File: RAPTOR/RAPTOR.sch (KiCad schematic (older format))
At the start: 49 parts, among them J1 SOLC_CONN, J10 EXT_LED3, J11 SRVOL_CONN, J12 SRVOR_CONN, J13 HOTWIRE_CONN, J14 RBF_CONN, J15 EEPROM_BTN_CONN, J16 SOLC_SW_CONN, J17 SOLP_SW_CONN, J18 CONN_BUZZER, J2 SOLP_CONN, J3 JST_2MM_MALE, J4 CONN_LED_FIX, J5 CONN_SOLP_LED, J6 CONN_SOLC_LED, J7 EXT_LED0, J8 EXT_LED1, J9 EXT_LED2, P1 Power, P2 Analog, P3 Digital, P4 Digital, P5 CONN_01X01, P6 CONN_01X01, P7 CONN_01X01, P8 CONN_01X01, Q1 MOSFET-NCH-STQ2NK60ZR-AP, Q2 MOSFET-NCH-STQ2NK60ZR-AP, Q3 MOSFET-NCH-STQ2NK60ZR-AP, Q4 MOSFET-NCH-STQ2NK60ZR-AP, Q5 MOSFET-NCH-STQ2NK60ZR-AP, U1 BMP280 Breakout, U2 BNO055 Breakout, U3 OpenLog, U4 AdafruitGPS, U5 U3V12F12, U6 D24V550F5

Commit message: do schematic for thunderbird
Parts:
- removed D8, D9: DIODE-1N4148, Silicon-Custom:DIODE-1N4148, symbol RAPTOR-rescue:DIODE-1N4148-SparkFun-DiscreteSemi
- removed J1: SOLC_CONN, RAPTOR_footprints:Molex-2pin, symbol RAPTOR-rescue:CONN_02-SparkFun-Connectors
- removed J12: SRVOR_CONN, RAPTOR_footprints:Molex-MOTOR, symbol RAPTOR-rescue:CONN_03-SparkFun-Connectors
- removed J13: HOTWIRE_CONN, RAPTOR_footprints:Molex-2pin, symbol RAPTOR-rescue:CONN_02-SparkFun-Connectors
- removed J16: SOLC_SW_CONN, RAPTOR_footprints:Molex-2pin, symbol RAPTOR-rescue:CONN_02-SparkFun-Connectors
- removed J17: SOLP_SW_CONN, RAPTOR_footprints:Molex-2pin, symbol RAPTOR-rescue:CONN_02-SparkFun-Connectors
- removed J2: SOLP_CONN, RAPTOR_footprints:Molex-2pin, symbol RAPTOR-rescue:CONN_02-SparkFun-Connectors
- removed J4: CONN_LED_FIX, RAPTOR_footprints:Molex-2pin, symbol RAPTOR-rescue:CONN_02-SparkFun-Connectors
- removed J5: CONN_SOLP_LED, RAPTOR_footprints:Molex-2pin, symbol RAPTOR-rescue:CONN_02-SparkFun-Connectors
- removed J6: CONN_SOLC_LED, RAPTOR_footprints:Molex-2pin, symbol RAPTOR-rescue:CONN_02-SparkFun-Connectors
- removed JP1, JP2: Jumper, symbol Device:Jumper
- removed P1: Power, RAPTOR_footprints:Socket_Strip_Arduino_1x08, symbol Connector_Generic:Conn_01x08
- removed P2: Analog, RAPTOR_footprints:Arduino_Analog_06, symbol RAPTOR-rescue:Arduino_Analog_Conn
- removed P3: Digital, RAPTOR_footprints:Arduino_x10_Digital, symbol RAPTOR-rescue:Arduino_Digital_01x10_Conn
- removed P4: Digital, RAPTOR_footprints:Arduino_x08_Digital, symbol RAPTOR-rescue:Arduino_Digital_8
- removed P5, P6, P7, P8: CONN_01X01, Socket_Arduino_Uno:Arduino_1pin, symbol Connector_Generic:Conn_01x01
- removed Q1, Q2, Q5: MOSFET-NCH-STQ2NK60ZR-AP, RAPTOR_footprints:MOSFET, symbol RAPTOR-rescue:MOSFET-NCH-2N7002PW-SparkFun-DiscreteSemi
- removed R2, R3, R4: 100OHM-0603-1_10W-1%, RAPTOR_footprints:Resistor, symbol RAPTOR-rescue:100OHM-0603-1_10W-1%-SparkFun-Resistors
- removed R6, R7, R8: 4.7KOHM-0603-1_10W-1%, RAPTOR_footprints:Resistor, symbol RAPTOR-rescue:4.7KOHM-0603-1_10W-1%-SparkFun-Resistors
- removed U1: BMP280 Breakout, RAPTOR_footprints:BMP280, symbol RAPTOR-rescue:BMP280-bmp280
- removed U2: BNO055 Breakout, RAPTOR_footprints:BNO055, symbol RAPTOR-rescue:BNO055-bno055
- removed U3: OpenLog, RAPTOR_footprints:OpenLog, symbol RAPTOR-rescue:OpenLog-openlog
- removed U5: U3V12F12, RAPTOR_footprints:U3V12F12, symbol RAPTOR-rescue:U3V12F12
- added A?: Arduino_Nano_v3.x, Module:Arduino_Nano, symbol MCU_Module:Arduino_Nano_v3.x
- added U?: microsd, symbol RAPTOR-rescue:microsd
- J11: value SRVOL_CONN -> SRVO_CONN
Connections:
- net labels added: MISO, MOSI, SCK, SRVO, SS
- net labels removed: +12V, A4(SDA), A5(SCL), AREF, HOTWIRE, I2C_SCL, I2C_SDA, IOREF, LEDC_DTA, LEDP_DTA, Reset, SD_RX, SD_TX, SOLC_DTA, SOLC_SW, SOLP_DTA, SOLP_SW, SRVO_L, SRVO_R
- wire segments 182 -> 83
- no-connect marks 18 -> 6
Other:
- note removed: "1"
- note removed: "Holes"
- note removed: "Shield for Arduino that uses\nthe same pin disposition\nlike "Uno" board Rev 3."
- moved on the sheet: J10, J11, J14, J15, J18, J3, J7, J8, J9, Q3, Q4, R1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

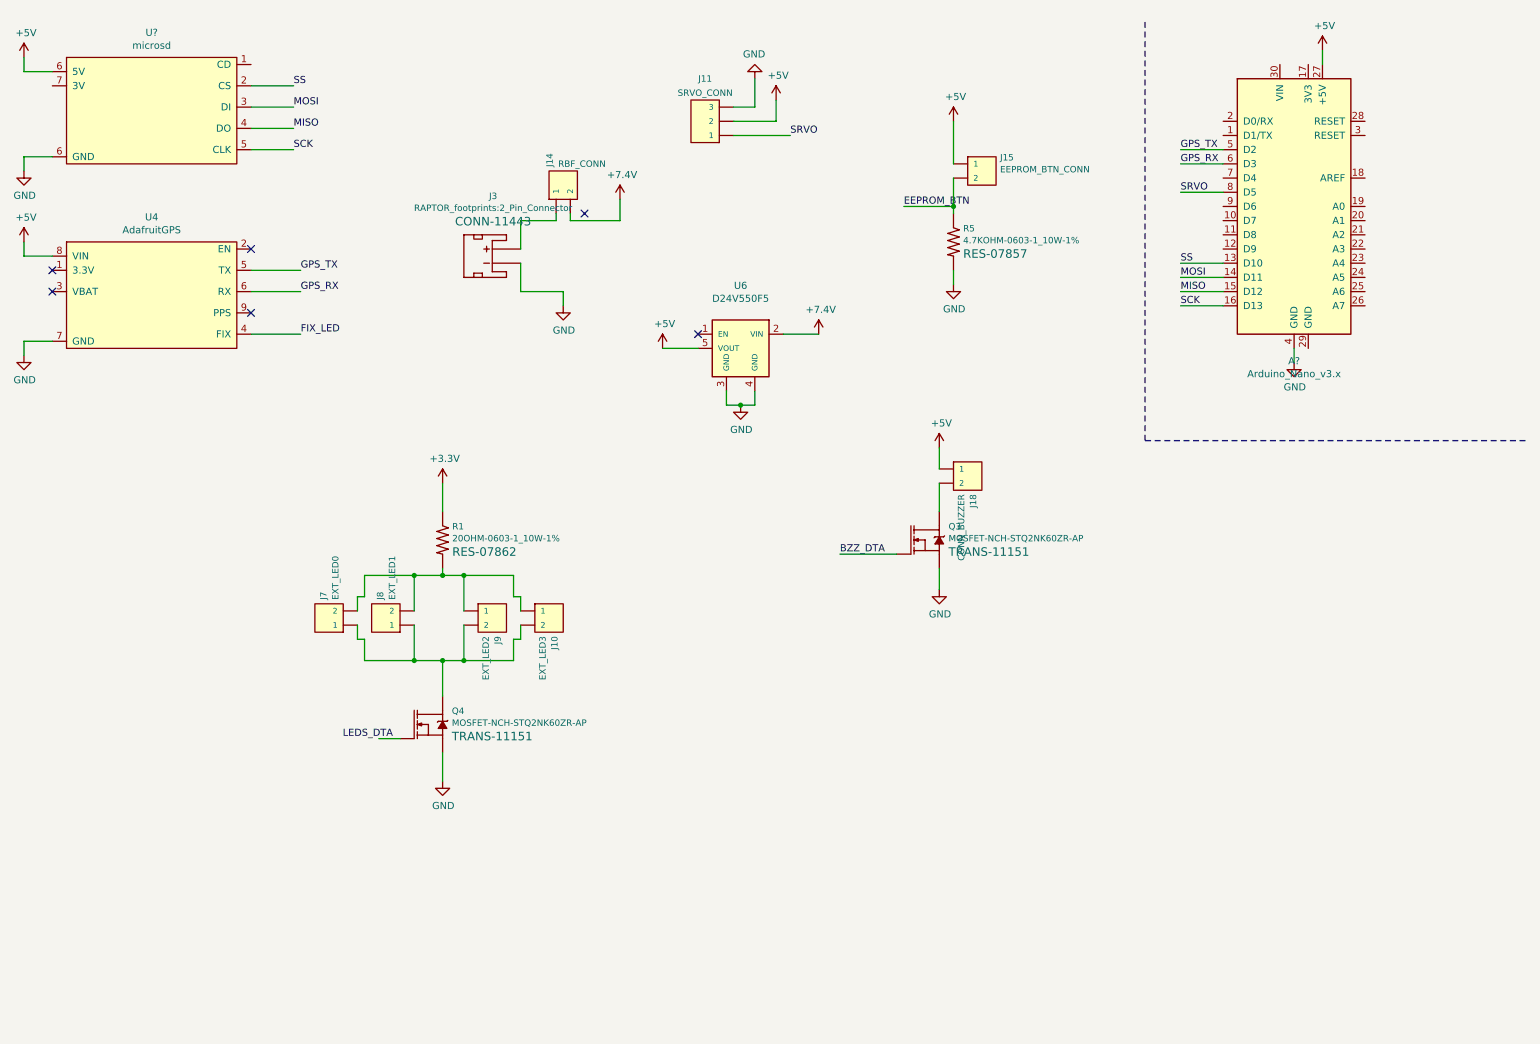
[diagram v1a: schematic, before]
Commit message: update schematic, remove some leds and eeprom button
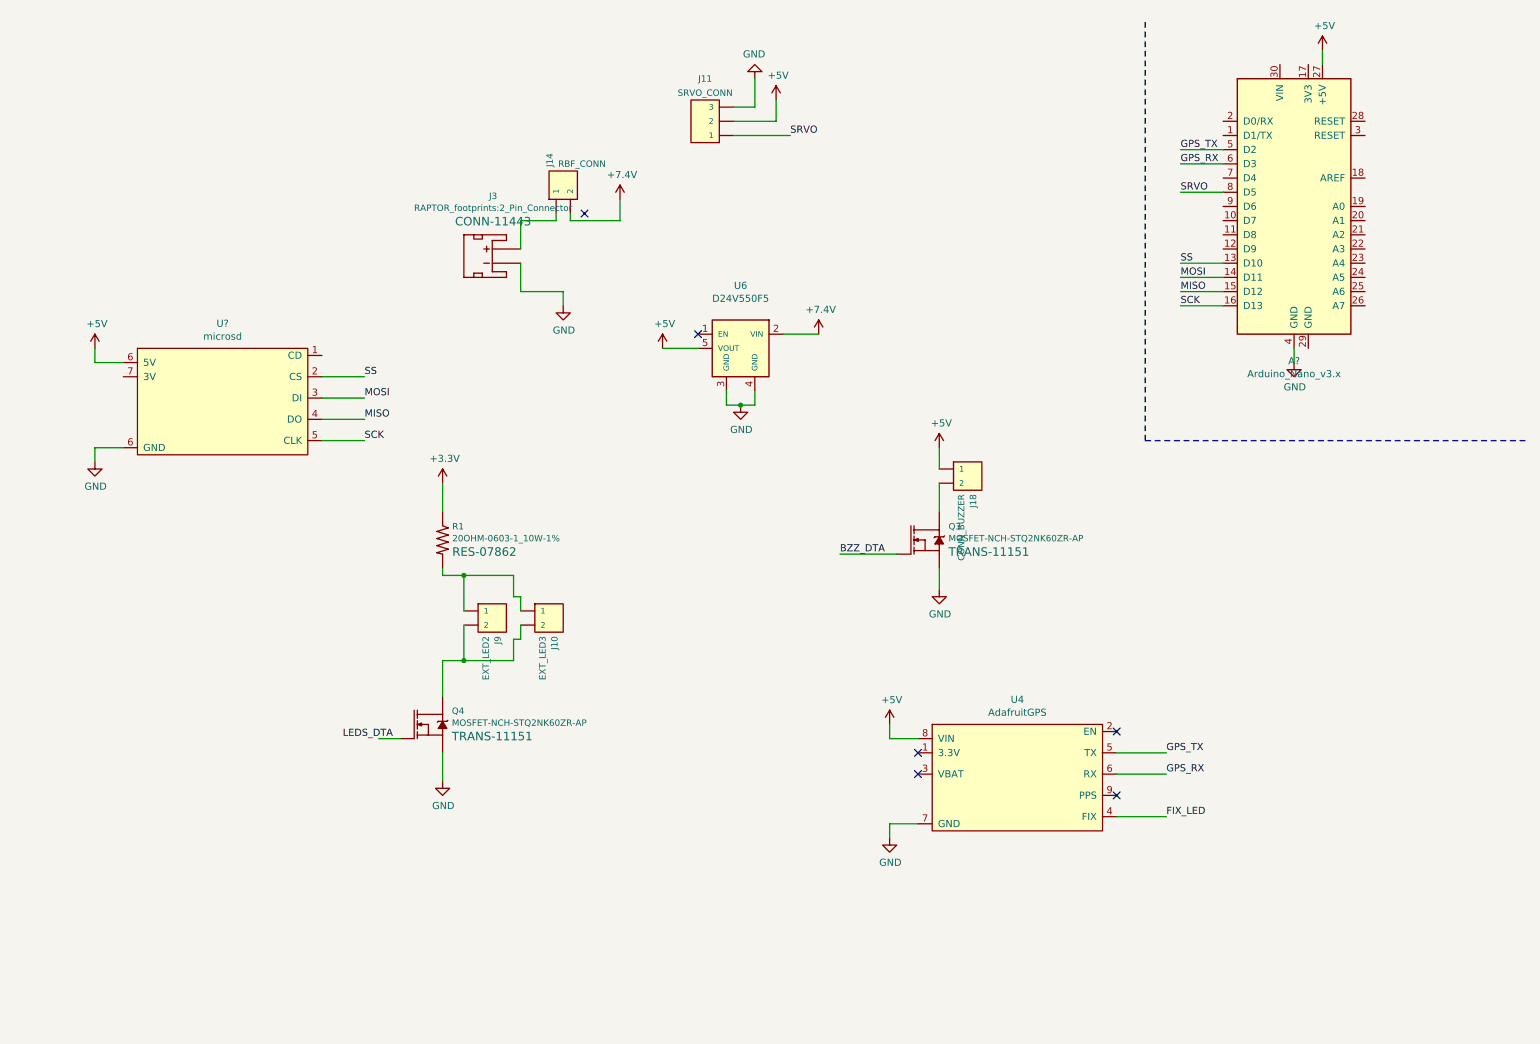
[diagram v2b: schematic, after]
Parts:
- removed J15: EEPROM_BTN_CONN, RAPTOR_footprints:Molex-2pin, symbol RAPTOR-rescue:CONN_02-SparkFun-Connectors
- removed J7: EXT_LED0, RAPTOR_footprints:Molex-2pin, symbol RAPTOR-rescue:CONN_02-SparkFun-Connectors
- removed J8: EXT_LED1, RAPTOR_footprints:Molex-2pin, symbol RAPTOR-rescue:CONN_02-SparkFun-Connectors
- removed R5: 4.7KOHM-0603-1_10W-1%, RAPTOR_footprints:Resistor, symbol RAPTOR-rescue:4.7KOHM-0603-1_10W-1%-SparkFun-Resistors
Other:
- moved on the sheet: U4, U?
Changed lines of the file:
@@
 L RAPTOR-rescue:AdafruitGPS-adafruitgps U4
 U 1 1 5BDE25E6
-P 1500 2400
-F 0 "U4" H 1500 2925 50  0000 C CNN
-F 1 "AdafruitGPS" H 1500 2834 50  0000 C CNN
-F 2 "RAPTOR_footprints:AdafruitGPS" H 1600 2350 50  0001 C CNN
-F 3 "https://learn.adafruit.com/adafruit-ultimate-gps" H 1600 2350 50  0001 C CNN
-	1    1500 2400
+P 7600 5800
+F 0 "U4" H 7600 6325 50  0000 C CNN
+F 1 "AdafruitGPS" H 7600 6234 50  0000 C CNN
+F 2 "RAPTOR_footprints:AdafruitGPS" H 7700 5750 50  0001 C CNN
+F 3 "https://learn.adafruit.com/adafruit-ultimate-gps" H 7700 5750 50  0001 C CNN
+	1    7600 5800
 	1    0    0    -1
 $EndComp
@@
 L power:GND #PWR0106
 U 1 1 5BDE7CE6
-P 600 2850
-F 0 "#PWR0106" H 600 2600 50  0001 C CNN
-F 1 "GND" H 605 2677 50  0000 C CNN
-F 2 "" H 600 2850 50  0001 C CNN
-F 3 "" H 600 2850 50  0001 C CNN
-	1    600  2850
-	1    0    0    -1
-$EndComp
-Wire Wire Line
-	800  2750 600  2750
-Wire Wire Line
-	600  2750 600  2850
+P 6700 6250
+F 0 "#PWR0106" H 6700 6000 50  0001 C CNN
+F 1 "GND" H 6705 6077 50  0000 C CNN
+F 2 "" H 6700 6250 50  0001 C CNN
+F 3 "" H 6700 6250 50  0001 C CNN
+	1    6700 6250
+	1    0    0    -1
+$EndComp
+Wire Wire Line
+	6900 6150 6700 6150
+Wire Wire Line
+	6700 6150 6700 6250
 $Comp
 L power:+5V #PWR0107
 U 1 1 5BDE90FA
-P 600 2050
-F 0 "#PWR0107" H 600 1900 50  0001 C CNN
-F 1 "+5V" H 615 2223 50  0000 C CNN
-F 2 "" H 600 2050 50  0001 C CNN
-F 3 "" H 600 2050 50  0001 C CNN
-	1    600  2050
-	1    0    0    -1
-$EndComp
-Wire Wire Line
-	600  2050 600  2150
-Wire Wire Line
-	600  2150 800  2150
-Text Label 2550 2250 0    50   ~ 0
+P 6700 5450
+F 0 "#PWR0107" H 6700 5300 50  0001 C CNN
+F 1 "+5V" H 6715 5623 50  0000 C CNN
+F 2 "" H 6700 5450 50  0001 C CNN
+F 3 "" H 6700 5450 50  0001 C CNN
+	1    6700 5450
+	1    0    0    -1
+$EndComp
+Wire Wire Line
+	6700 5450 6700 5550
+Wire Wire Line
+	6700 5550 6900 5550
+Text Label 8650 5650 0    50   ~ 0
 GPS_TX
 Wire Wire Line
-	2200 2250 2550 2250
-Text Label 2550 2400 0    50   ~ 0
+	8300 5650 8650 5650
+Text Label 8650 5800 0    50   ~ 0
 GPS_RX
 Wire Wire Line
-	2200 2400 2550 2400
-Text Label 2550 2700 0    50   ~ 0
+	8300 5800 8650 5800
+Text Label 8650 6100 0    50   ~ 0
 FIX_LED
 Wire Wire Line
-	2200 2700 2550 2700
-NoConn ~ 800  2250
-NoConn ~ 800  2400
-NoConn ~ 2200 2550
-NoConn ~ 2200 2100
+	8300 6100 8650 6100
+NoConn ~ 6900 5650
+NoConn ~ 6900 5800
+NoConn ~ 8300 5950
+NoConn ~ 8300 5500
 Text Label 6000 1300 0    50   ~ 0
 SRVO
@@
 	4100 1900 4100 2100
 $Comp
-L power:+5V #PWR021
-U 1 1 5C539DC6
-P 7150 1200
-F 0 "#PWR021" H 7150 1050 50  0001 C CNN
-F 1 "+5V" H 7165 1373 50  0000 C CNN
-F 2 "" H 7150 1200 50  0001 C CNN
-F 3 "" H 7150 1200 50  0001 C CNN
-	1    7150 1200
-	1    0    0    -1
-$EndComp
-$Comp
-L power:GND #PWR022
-U 1 1 5C539DCC
-P 7150 2350
-F 0 "#PWR022" H 7150 2100 50  0001 C CNN
-F 1 "GND" H 7155 2177 50  0000 C CNN
-F 2 "" H 7150 2350 50  0001 C CNN
-F 3 "" H 7150 2350 50  0001 C CNN
-	1    7150 2350
-	1    0    0    -1
-$EndComp
-$Comp
-L RAPTOR-rescue:4.7KOHM-0603-1_10W-1%-SparkFun-Resistors R5
-U 1 1 5C539DD3
-P 7150 2050
-F 0 "R5" V 7055 2118 45  0000 L CNN
-F 1 "4.7KOHM-0603-1_10W-1%" V 7139 2118 45  0000 L CNN
-F 2 "RAPTOR_footprints:Resistor" H 7150 2200 20  0001 C CNN
-F 3 "" H 7150 2050 60  0001 C CNN
-F 4 "RES-07857" V 7234 2118 60  0000 L CNN "Field4"
-	1    7150 2050
-	0    1    1    0
-$EndComp
-Wire Wire Line
-	7150 2250 7150 2350
-$Comp
 L RAPTOR-rescue:CONN_03-SparkFun-Connectors J11
 U 1 1 5C6B1587
@@
 	3700 5000 4050 5000
 Wire Wire Line
-	3000 4850 3000 5000
-Wire Wire Line
-	3000 5000 3350 5000
-Connection ~ 3350 5000
-Wire Wire Line
-	3000 4550 3000 4400
-Wire Wire Line
-	3000 4400 3350 4400
-Wire Wire Line
 	3550 4400 3550 4350
-Connection ~ 3350 4400
-Wire Wire Line
-	3350 4400 3550 4400
 Wire Wire Line
 	3700 4400 3550 4400
-Connection ~ 3550 4400
 Wire Wire Line
 	4050 4550 4050 4400
@@
 	-1   0    0    1
 $EndComp
-$Comp
-L RAPTOR-rescue:CONN_02-SparkFun-Connectors J8
-U 1 1 5C557DC0
-P 3250 4750
-F 0 "J8" V 3111 4928 45  0000 L CNN
-F 1 "EXT_LED1" V 3195 4928 45  0000 L CNN
-F 2 "RAPTOR_footprints:Molex-2pin" H 3250 5000 20  0001 C CNN
-F 3 "" H 3250 4750 50  0001 C CNN
-F 4 "XXX-00000" V 3290 4928 60  0001 L CNN "Field4"
-	1    3250 4750
-	1    0    0    -1
-$EndComp
-$Comp
-L RAPTOR-rescue:CONN_02-SparkFun-Connectors J7
-U 1 1 5C5688B4
-P 2850 4750
-F 0 "J7" V 2711 4928 45  0000 L CNN
-F 1 "EXT_LED0" V 2795 4928 45  0000 L CNN
-F 2 "RAPTOR_footprints:Molex-2pin" H 2850 5000 20  0001 C CNN
-F 3 "" H 2850 4750 50  0001 C CNN
-F 4 "XXX-00000" V 2890 4928 60  0001 L CNN "Field4"
-	1    2850 4750
-	1    0    0    -1
-$EndComp
 Wire Wire Line
 	4050 4550 4100 4550
@@
 	4100 4850 4100 4750
 Wire Wire Line
-	3000 4550 2950 4550
-Wire Wire Line
-	2950 4550 2950 4650
-Wire Wire Line
-	3000 4850 2950 4850
-Wire Wire Line
-	2950 4850 2950 4750
-Wire Wire Line
 	3700 4400 3700 4650
 Wire Wire Line
-	3350 4400 3350 4650
-Wire Wire Line
-	3350 4750 3350 5000
-Wire Wire Line
 	3700 4750 3700 5000
 Wire Wire Line
-	3350 5000 3550 5000
-Wire Wire Line
 	3550 5000 3550 5250
-Connection ~ 3550 5000
 Wire Wire Line
 	3550 5000 3700 5000
 Wire Wire Line
 	3550 5650 3550 5850
-$Comp
-L RAPTOR-rescue:CONN_02-SparkFun-Connectors J15
-U 1 1 5C767459
-P 7250 1500
-F 0 "J15" H 7022 1455 45  0000 R CNN
-F 1 "EEPROM_BTN_CONN" H 7022 1539 45  0000 R CNN
-F 2 "RAPTOR_footprints:Molex-2pin" H 7250 1750 20  0001 C CNN
-F 3 "" H 7250 1500 50  0001 C CNN
-F 4 "XXX-00000" H 7022 1634 60  0001 R CNN "Field4"
-	1    7250 1500
-	-1   0    0    1
-$EndComp
-Wire Wire Line
-	7150 1200 7150 1500
 NoConn ~ 4550 1850
 Wire Wire Line
@@
 	1    0    0    -1
 $EndComp
-Wire Wire Line
-	7150 1800 7150 1850
-Connection ~ 7150 1800
-Wire Wire Line
-	6800 1800 7150 1800
-Text Label 6800 1800 0    50   ~ 0
-EEPROM_BTN
 $Comp
 L RAPTOR-rescue:microsd U?
 U 1 1 5D34E005
-P 1500 1100
-F 0 "U?" H 1500 1625 50  0000 C CNN
-F 1 "microsd" H 1500 1534 50  0000 C CNN
-F 2 "" H 1500 1500 50  0001 C CNN
-F 3 "" H 1500 1500 50  0001 C CNN
-	1    1500 1100
-	1    0    0    -1
-$EndComp
-Wire Wire Line
-	600  850  800  850
+P 2000 3150
+F 0 "U?" H 2000 3675 50  0000 C CNN
+F 1 "microsd" H 2000 3584 50  0000 C CNN
+F 2 "" H 2000 3550 50  0001 C CNN
+F 3 "" H 2000 3550 50  0001 C CNN
+	1    2000 3150
+	1    0    0    -1
+$EndComp
+Wire Wire Line
+	1100 2900 1300 2900
 $Comp
 L power:GND #PWR?
 U 1 1 5D361F5D
-P 600 1550
-F 0 "#PWR?" H 600 1300 50  0001 C CNN
-F 1 "GND" H 605 1377 50  0000 C CNN
-F 2 "" H 600 1550 50  0001 C CNN
-F 3 "" H 600 1550 50  0001 C CNN
-	1    600  1550
-	1    0    0    -1
-$EndComp
-Wire Wire Line
-	800  1450 600  1450
-Wire Wire Line
-	600  1450 600  1550
-Text Label 2500 1400 0    50   ~ 0
+P 1100 3600
+F 0 "#PWR?" H 1100 3350 50  0001 C CNN
+F 1 "GND" H 1105 3427 50  0000 C CNN
+F 2 "" H 1100 3600 50  0001 C CNN
+F 3 "" H 1100 3600 50  0001 C CNN
+	1    1100 3600
+	1    0    0    -1
+$EndComp
+Wire Wire Line
+	1300 3500 1100 3500
+Wire Wire Line
+	1100 3500 1100 3600
+Text Label 3000 3450 0    50   ~ 0
 SCK
-Text Label 2500 1250 0    50   ~ 0
+Text Label 3000 3300 0    50   ~ 0
 MISO
-Text Label 2500 1100 0    50   ~ 0
+Text Label 3000 3150 0    50   ~ 0
 MOSI
-Text Label 2500 950  0    50   ~ 0
+Text Label 3000 3000 0    50   ~ 0
 SS
 Wire Wire Line
-	2200 950  2500 950
-Wire Wire Line
-	2200 1100 2500 1100
-Wire Wire Line
-	2200 1250 2500 1250
-Wire Wire Line
-	2200 1400 2500 1400
+	2700 3000 3000 3000
+Wire Wire Line
+	2700 3150 3000 3150
+Wire Wire Line
+	2700 3300 3000 3300
+Wire Wire Line
+	2700 3450 3000 3450
 Text Label 8750 2500 0    50   ~ 0
 SCK
@@
 Wire Wire Line
 	8750 1500 9050 1500
-Wire Wire Line
-	7150 1750 7150 1800
-Wire Wire Line
-	7150 1600 7150 1800
 Text Label 8750 1700 0    50   ~ 0
 SRVO
@@
 	8750 1700 9050 1700
 Wire Wire Line
-	600  750  600  850
+	1100 2800 1100 2900
 $Comp
 L power:+5V #PWR?
 U 1 1 5D3604B5
-P 600 750
-F 0 "#PWR?" H 600 600 50  0001 C CNN
-F 1 "+5V" H 615 923 50  0000 C CNN
-F 2 "" H 600 750 50  0001 C CNN
-F 3 "" H 600 750 50  0001 C CNN
-	1    600  750
-	1    0    0    -1
-$EndComp
+P 1100 2800
+F 0 "#PWR?" H 1100 2650 50  0001 C CNN
+F 1 "+5V" H 1115 2973 50  0000 C CNN
+F 2 "" H 1100 2800 50  0001 C CNN
+F 3 "" H 1100 2800 50  0001 C CNN
+	1    1100 2800
+	1    0    0    -1
+$EndComp
